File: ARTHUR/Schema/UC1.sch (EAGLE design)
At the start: 13 parts, among them U1 328P, Y1 16MHz

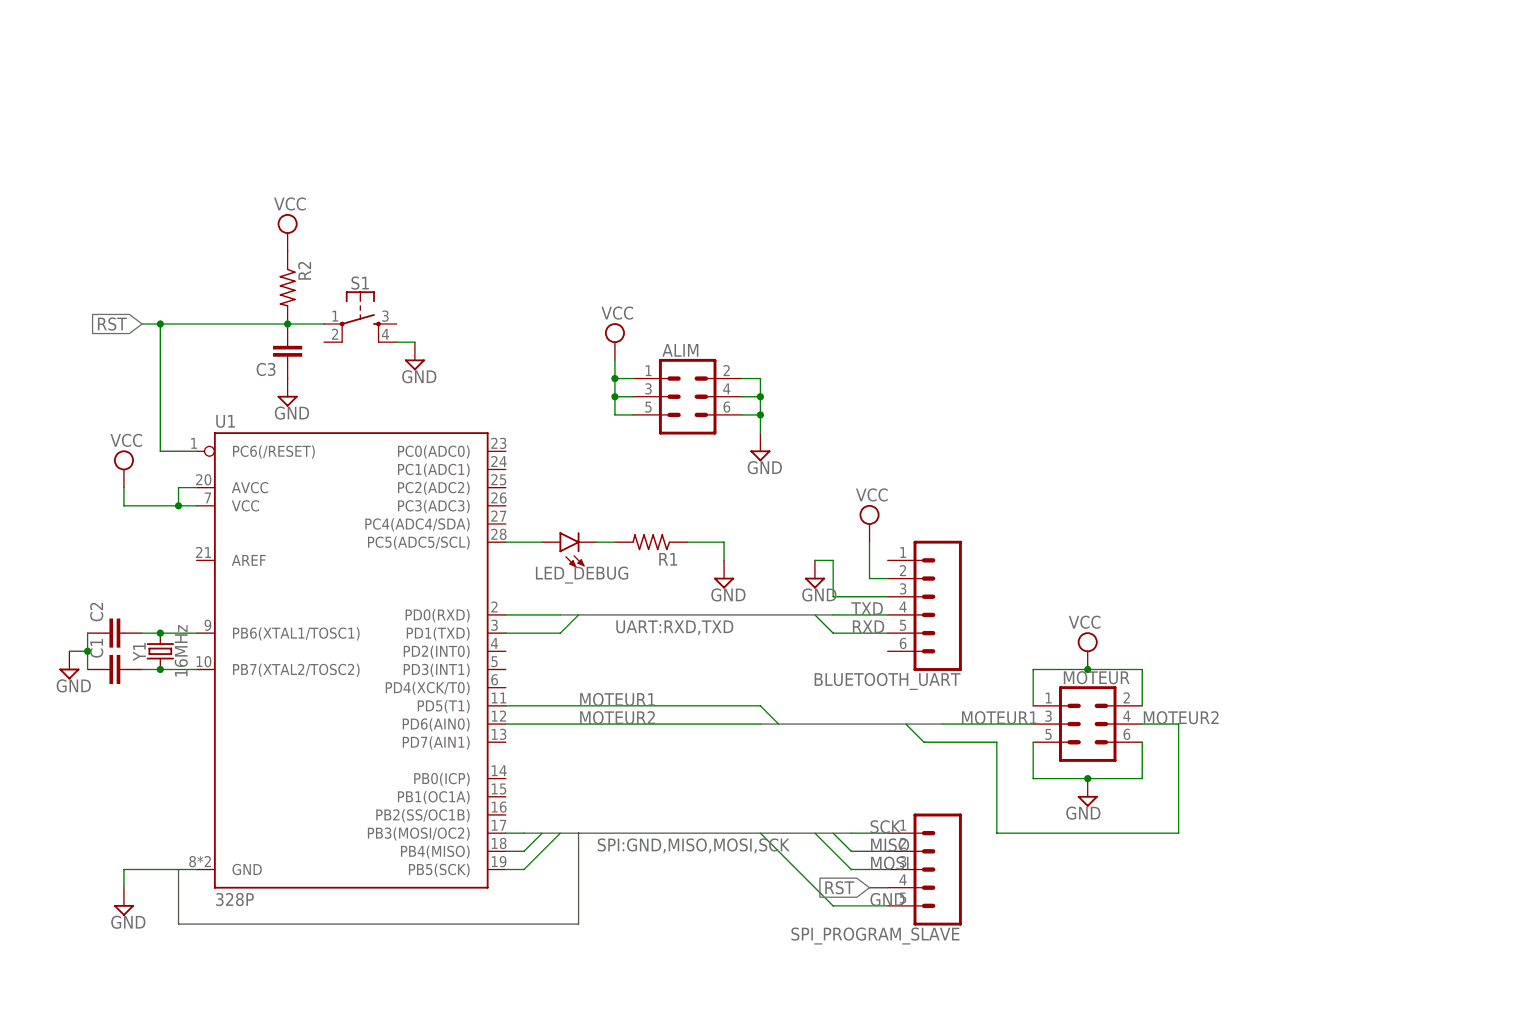
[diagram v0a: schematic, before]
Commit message: Nouveau schema electronique en concordance avec le nouveau programme pour les moteurs ;)
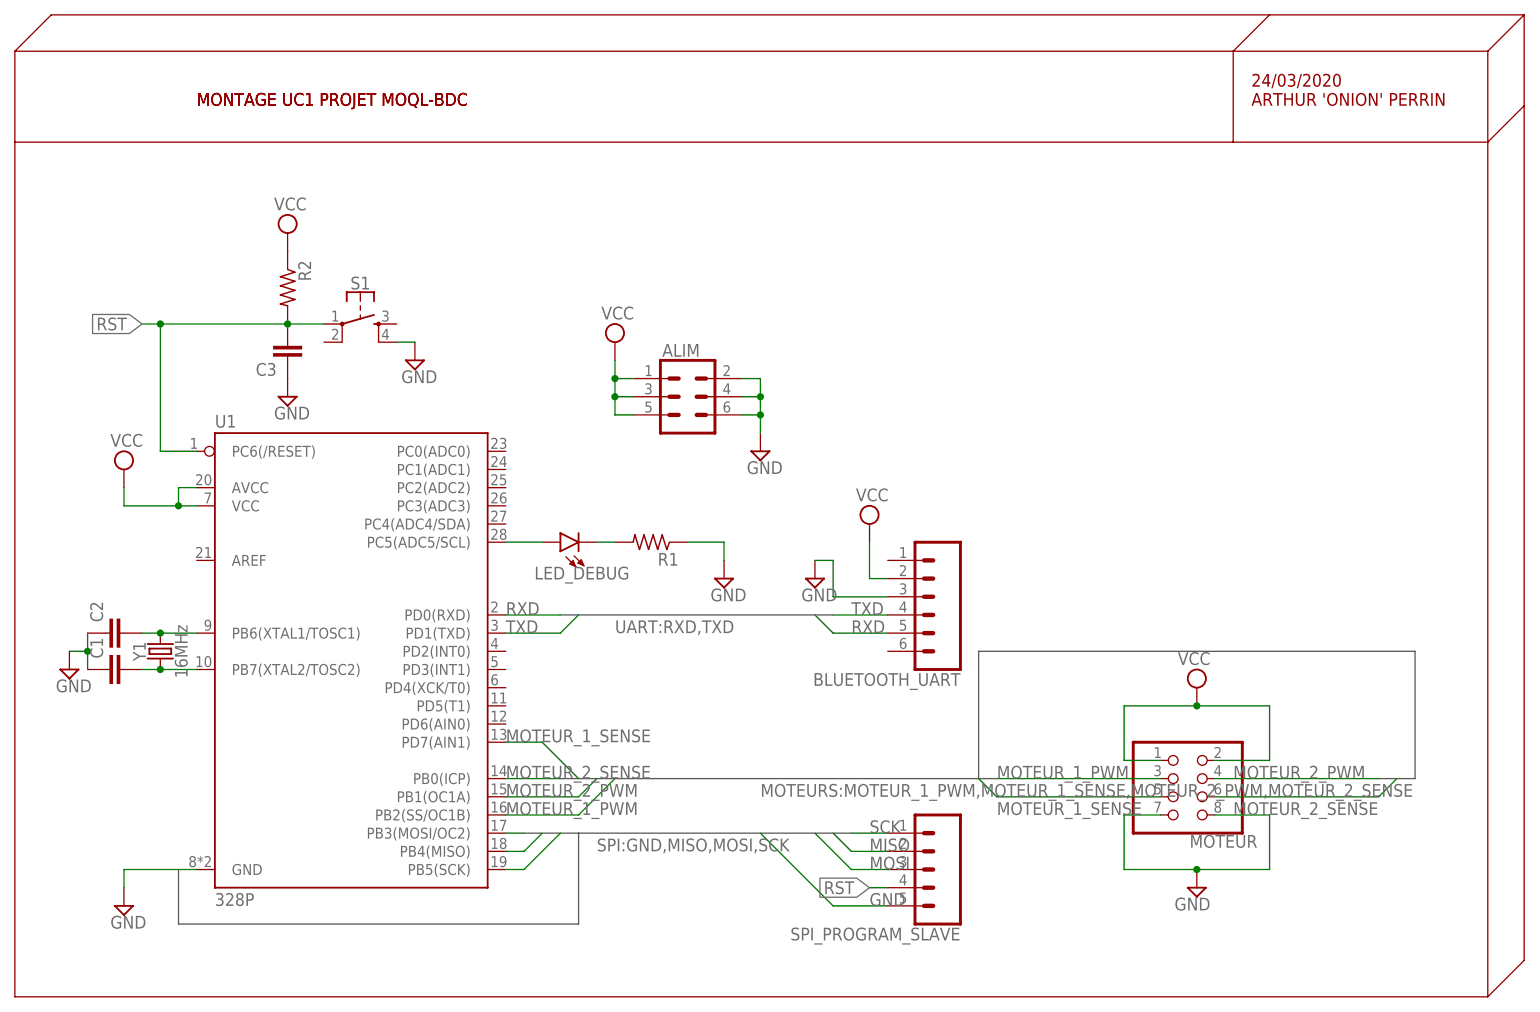
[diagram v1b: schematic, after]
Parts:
- MOTEUR: device SparkFun-Connectors:CONN_03X2FEMALE -> pinhead:PINHD-2X4
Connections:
- removed net MOTEUR1: MOTEUR.3, U1.PD5(T1)
- removed net MOTEUR2: MOTEUR.4, U1.PD6(AIN0)
- new net MOTEUR_1_PWM: MOTEUR.3, U1.PB2(SS/OC1B)
- new net MOTEUR_1_SENSE: MOTEUR.5, U1.PD7(AIN1)
- new net MOTEUR_2_PWM: MOTEUR.4, U1.PB1(OC1A)
- new net MOTEUR_2_SENSE: MOTEUR.6, U1.PB0(ICP)
- net GND: now also MOTEUR.7, MOTEUR.8; no longer MOTEUR.5, MOTEUR.6
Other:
- note added: "24/03/2020 ARTHUR 'ONION' PERRIN"
- note added: "MONTAGE UC1 PROJET MOQL-BDC"
